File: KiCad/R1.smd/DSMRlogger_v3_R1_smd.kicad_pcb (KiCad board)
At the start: 2 copper layers, 60 x 60 mm, 22 parts, among them J1 RJ11-6, J3 3v3, J4 5V, J5 GND, Q1 BC547, U1 MCP1700-3302E, U2 ESP-01

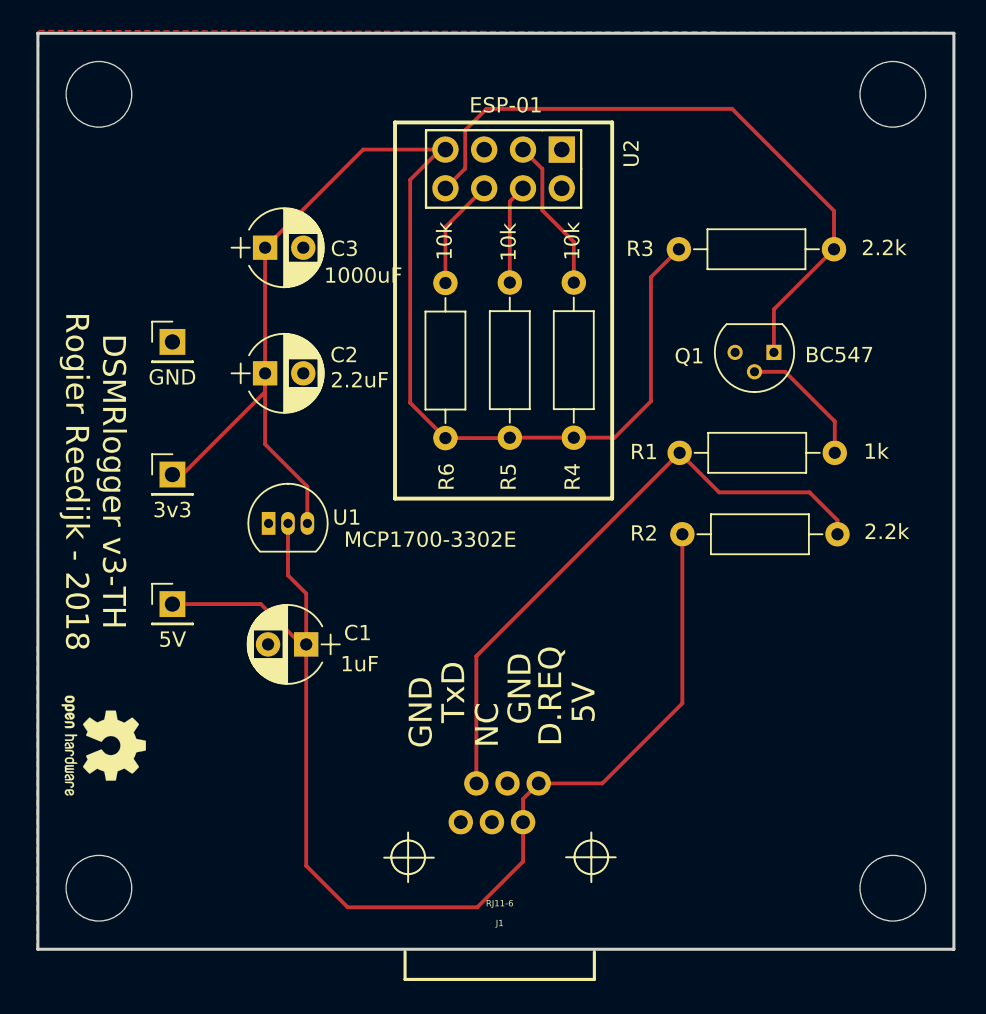
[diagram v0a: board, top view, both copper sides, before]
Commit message: Generated gerbers and improved layout pcb for hand soldering
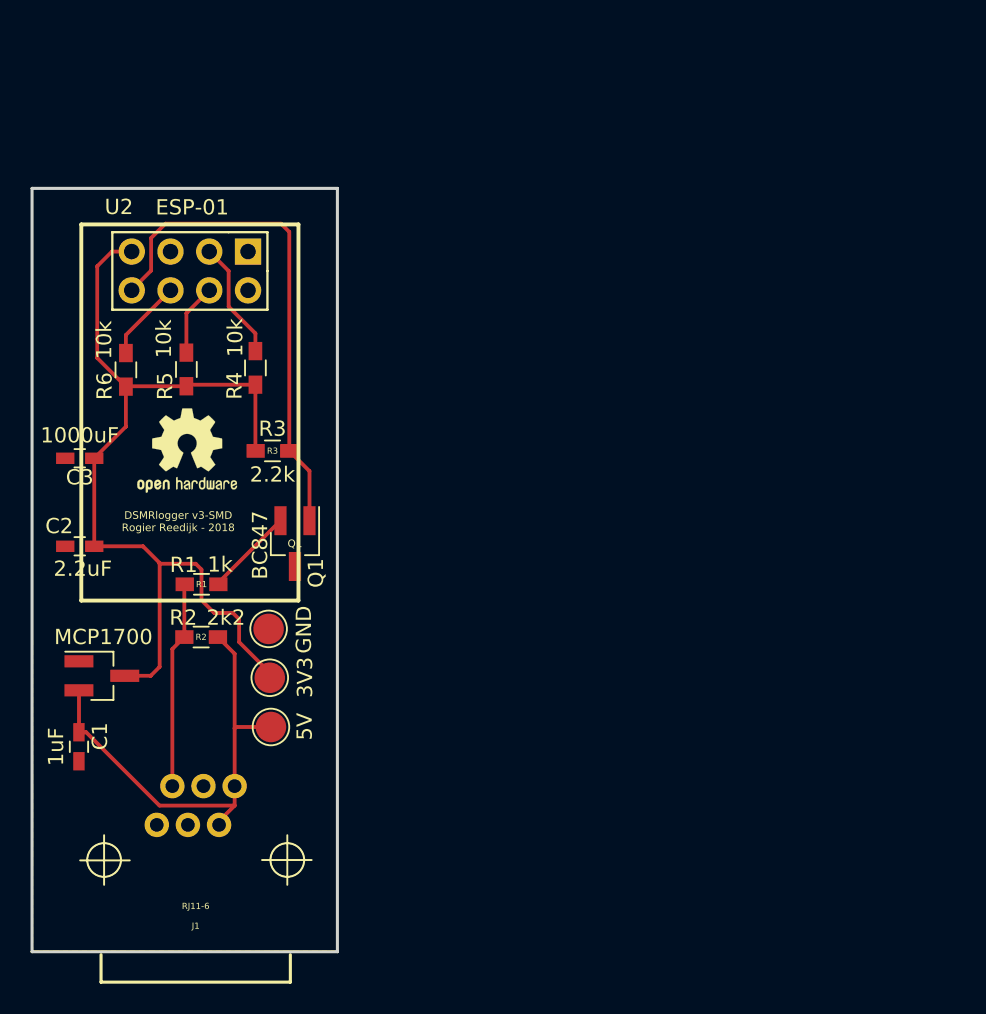
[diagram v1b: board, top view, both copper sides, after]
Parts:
- removed J3: 3v3, Pin_Headers:Pin_Header_Straight_1x01_Pitch2.54mm
- removed J4: 5V, Pin_Headers:Pin_Header_Straight_1x01_Pitch2.54mm
- removed J5: GND, Pin_Headers:Pin_Header_Straight_1x01_Pitch2.54mm
- removed REF** (x4): MountingHole_4.3mm_M4, Mounting_Holes:MountingHole_4.3mm_M4
- removed the REF*** at (104.3, 146.7)
- removed the REF*** at (104.3, 116.1)
- added REF***: OSHW-Logo2_7.3x6mm_SilkScreen, Symbols:OSHW-Logo2_7.3x6mm_SilkScreen, B.Cu at (109.2, 135.9)
- added REF***: OSHW-Logo2_7.3x6mm_SilkScreen, Symbols:OSHW-Logo2_7.3x6mm_SilkScreen, F.Cu at (109.8, 127.3)
- added TP3: 3V3, Connectors_TestPoints:Test_Point_Pad_d2.0mm, F.Cu at (115.2, 142.2)
- added TP4: 5V, Connectors_TestPoints:Test_Point_Pad_d2.0mm, F.Cu at (115.3, 145.4)
- added TP5: GND, Connectors_TestPoints:Test_Point_Pad_d2.0mm, F.Cu at (115.1, 139.0)
- C1, C2, C3: footprint Capacitors_THT:CP_Radial_D5.0mm_P2.50mm -> Capacitors_SMD:C_0603_HandSoldering
- Q1: value BC547 -> BC847; footprint TO_SOT_Packages_THT:TO-92_Molded_Narrow -> TO_SOT_Packages_SMD:SOT-23_Handsoldering
- R1, R3, R4, R5, R6: footprint Resistors_THT:R_Axial_DIN0207_L6.3mm_D2.5mm_P10.16mm_Horizontal -> Resistors_SMD:R_0603_HandSoldering
- R2: value 2.2k -> 2k2; footprint Resistors_THT:R_Axial_DIN0207_L6.3mm_D2.5mm_P10.16mm_Horizontal -> Resistors_SMD:R_0603_HandSoldering
- U1: value MCP1700-3302E -> MCP1700; footprint TO_SOT_Packages_THT:TO-92_Inline_Narrow_Oval -> TO_SOT_Packages_SMD:SOT-23_Handsoldering
- moved R1 42.4 mm to (110.7, 136.1)
- moved R2 42.2 mm to (110.7, 139.5), turned to 0 degrees
- moved Q1 33.8 mm to (116.8, 133.4), turned to 270 degrees
- moved R3 29.7 mm to (115.4, 127.4)
- moved R5 21.7 mm to (109.7, 122.0)
- moved U2 21.6 mm to (113.8, 114.3)
- moved R6 21.4 mm to (105.8, 122.0)
- moved R4 21.3 mm to (114.2, 121.9)
- moved J1 19.9 mm to (110.3, 154.2)
- moved C3 18.4 mm to (102.7, 127.8), turned to 180 degrees
- moved C2 16.6 mm to (102.7, 133.6), turned to 180 degrees
- moved C1 16.3 mm to (102.7, 146.7), turned to 270 degrees
- moved U1 14.8 mm to (104.2, 142.1)
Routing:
- net 5V: track 77.5 -> 30.5 mm
- net 3V3: track 88.9 -> 62.1 mm
- net TxD: track 40.3 -> 13.6 mm
- net RxD: track 42.7 -> 33.1 mm
- net Net-(Q1-Pad2): track 8.66 -> 5.85 mm
- net Net-(R4-Pad2): track 10.1 -> 7.77 mm
- net Net-(R6-Pad2): track 7.25 -> 5.32 mm
- net Net-(R5-Pad2): track 6.53 -> 4.70 mm
- added copper zone on B.Cu, net GND
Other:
- board size 60 x 60 mm -> 20 x 50 mm
- board text added: "DSMRlogger v3-SMD Rogier Reedijk - 2018"
- board text removed: "DSMRlogger v3-TH Rogier Reedijk - 2018"
